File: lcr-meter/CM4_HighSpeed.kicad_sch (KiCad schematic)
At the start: 10 parts, among them J15 Conn_01x22_Female, J16 Conn_01x22_Female, J22 690-019-298-412, J6 THD-02-R, U12 RT9742SNGV

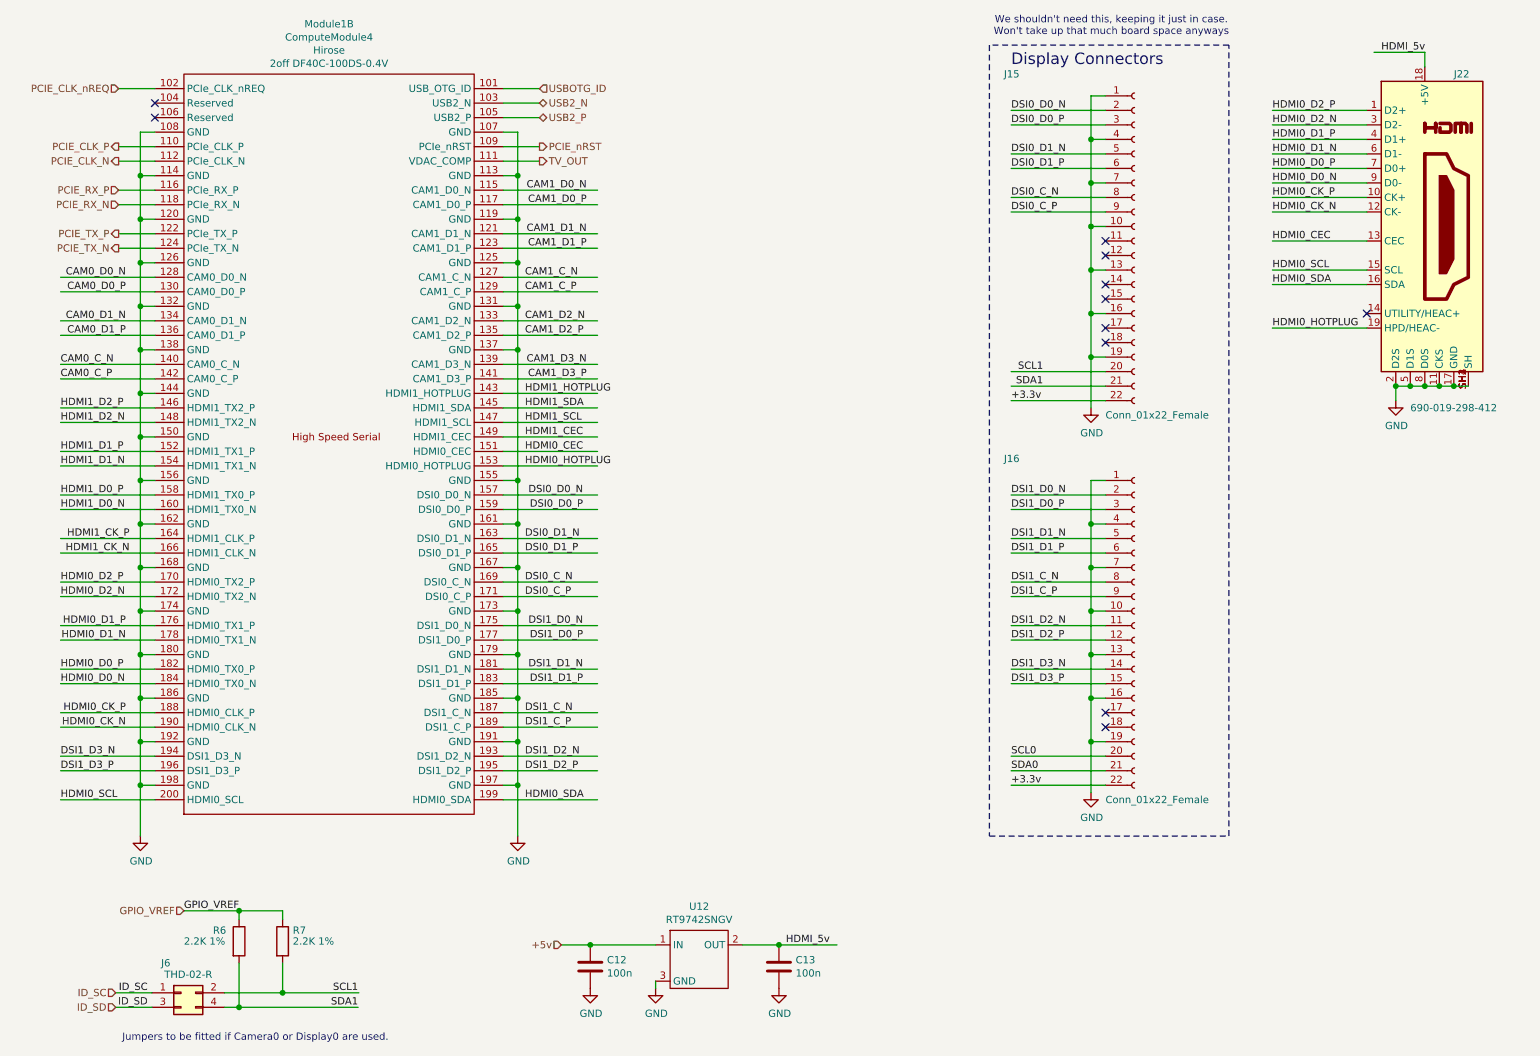
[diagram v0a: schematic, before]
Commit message: Progress, removal of unnecessary components
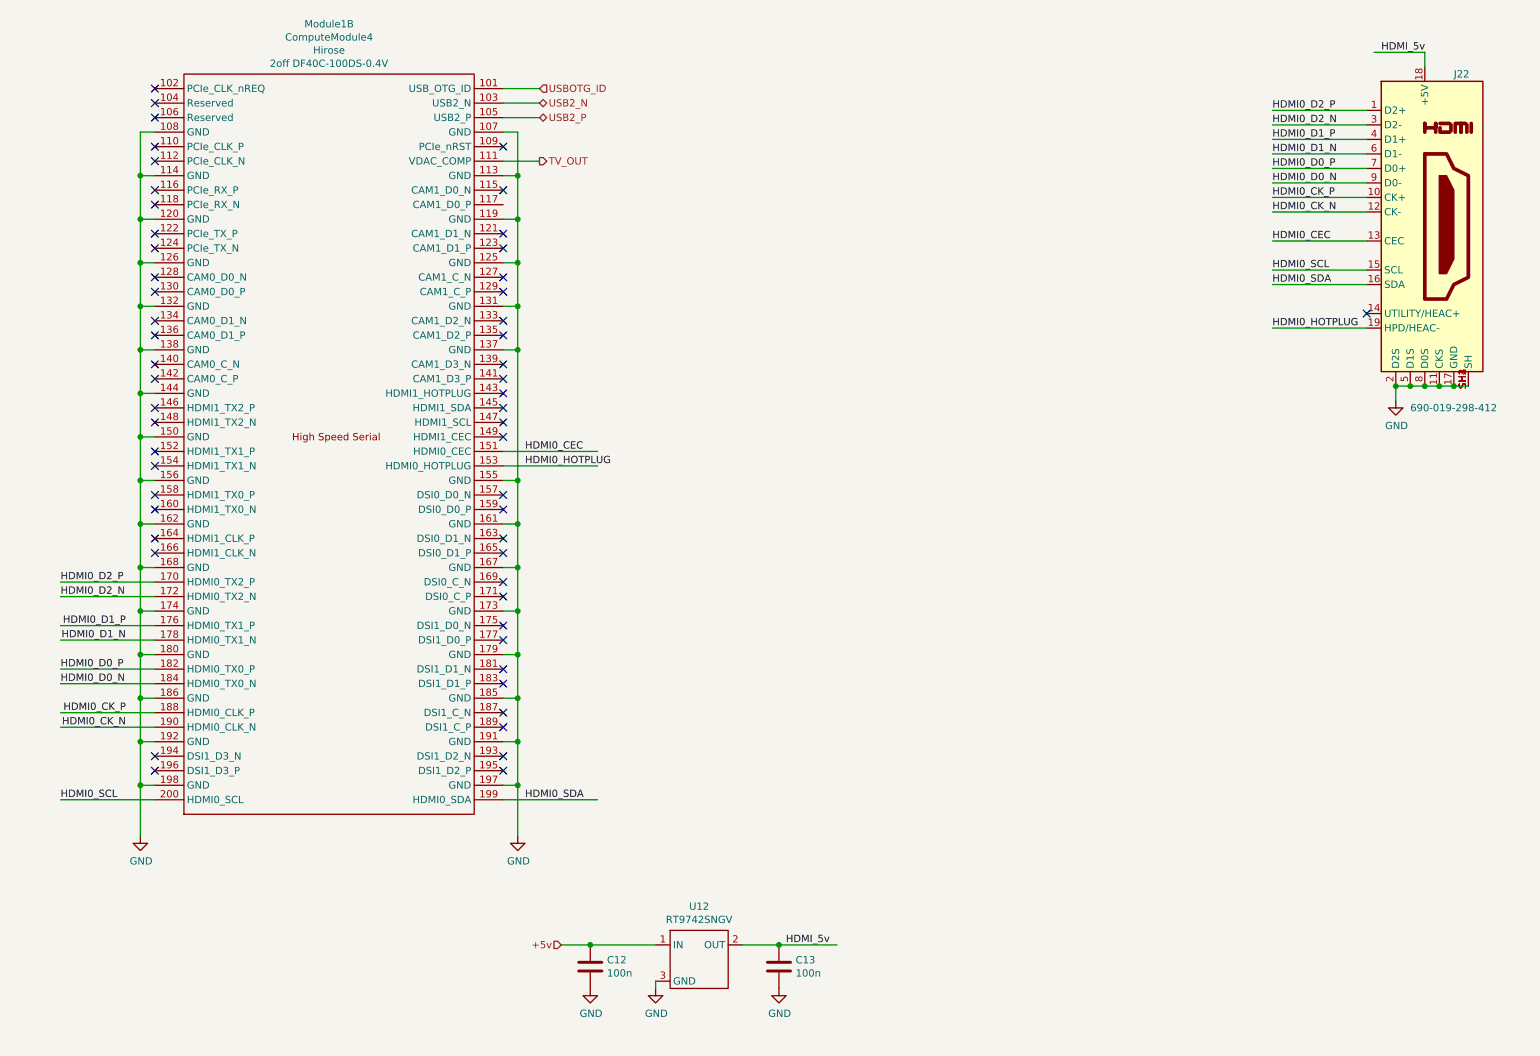
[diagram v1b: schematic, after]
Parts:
- removed J15, J16: Conn_01x22_Female, CM4IO:Hirose_FH12-22S-0.5SH_1x22-1MP_P0.50mm_Horizontal, symbol Connector:Conn_01x22_Female
- removed J6: THD-02-R, Connector_PinHeader_2.54mm:PinHeader_2x02_P2.54mm_Vertical, symbol Connector_Generic:Conn_02x02_Odd_Even
- removed R6, R7: 2.2K 1%, Resistor_SMD:R_0402_1005Metric, symbol Device:R
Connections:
- net CAM0_C_N: no longer names the net of Module1.140 (CAM0_C_N)
- net CAM0_C_P: no longer names the net of Module1.142 (CAM0_C_P)
- net CAM0_D0_N: no longer names the net of Module1.128 (CAM0_D0_N)
- net CAM0_D0_P: no longer names the net of Module1.130 (CAM0_D0_P)
- net CAM0_D1_N: no longer names the net of Module1.134 (CAM0_D1_N)
- net CAM0_D1_P: no longer names the net of Module1.136 (CAM0_D1_P)
- net CAM1_C_N: no longer names the net of Module1.127 (CAM1_C_N)
- net CAM1_C_P: no longer names the net of Module1.129 (CAM1_C_P)
- net CAM1_D0_N: no longer names the net of Module1.115 (CAM1_D0_N)
- net CAM1_D0_P: no longer names the net of Module1.117 (CAM1_D0_P)
- net CAM1_D1_N: no longer names the net of Module1.121 (CAM1_D1_N)
- net CAM1_D1_P: no longer names the net of Module1.123 (CAM1_D1_P)
- net CAM1_D2_N: no longer names the net of Module1.133 (CAM1_D2_N)
- net CAM1_D2_P: no longer names the net of Module1.135 (CAM1_D2_P)
- net CAM1_D3_N: no longer names the net of Module1.139 (CAM1_D3_N)
- net CAM1_D3_P: no longer names the net of Module1.141 (CAM1_D3_P)
- net DSI0_C_N: no longer names the net of Module1.169 (DSI0_C_N)
- net DSI0_C_P: no longer names the net of Module1.171 (DSI0_C_P)
- net DSI0_D0_N: no longer names the net of Module1.157 (DSI0_D0_N)
- net DSI0_D0_P: no longer names the net of Module1.159 (DSI0_D0_P)
- net DSI0_D1_N: no longer names the net of Module1.163 (DSI0_D1_N)
- net DSI0_D1_P: no longer names the net of Module1.165 (DSI0_D1_P)
- net DSI1_C_N: no longer names the net of Module1.187 (DSI1_C_N)
- net DSI1_C_P: no longer names the net of Module1.189 (DSI1_C_P)
- net DSI1_D0_N: no longer names the net of Module1.175 (DSI1_D0_N)
- net DSI1_D0_P: no longer names the net of Module1.177 (DSI1_D0_P)
- net DSI1_D1_N: no longer names the net of Module1.181 (DSI1_D1_N)
- net DSI1_D1_P: no longer names the net of Module1.183 (DSI1_D1_P)
- net DSI1_D2_N: no longer names the net of Module1.193 (DSI1_D2_N)
- net DSI1_D2_P: no longer names the net of Module1.195 (DSI1_D2_P)
- net DSI1_D3_N: no longer names the net of Module1.194 (DSI1_D3_N)
- net DSI1_D3_P: no longer names the net of Module1.196 (DSI1_D3_P)
- net HDMI1_CEC: no longer names the net of Module1.149 (HDMI1_CEC)
- net HDMI1_CK_N: no longer names the net of Module1.166 (HDMI1_CLK_N)
- net HDMI1_CK_P: no longer names the net of Module1.164 (HDMI1_CLK_P)
- net HDMI1_D0_N: no longer names the net of Module1.160 (HDMI1_TX0_N)
- net HDMI1_D0_P: no longer names the net of Module1.158 (HDMI1_TX0_P)
- net HDMI1_D1_N: no longer names the net of Module1.154 (HDMI1_TX1_N)
- net HDMI1_D1_P: no longer names the net of Module1.152 (HDMI1_TX1_P)
- net HDMI1_D2_N: no longer names the net of Module1.148 (HDMI1_TX2_N)
- net HDMI1_D2_P: no longer names the net of Module1.146 (HDMI1_TX2_P)
- net HDMI1_HOTPLUG: no longer names the net of Module1.143 (HDMI1_HOTPLUG)
- net HDMI1_SCL: no longer names the net of Module1.147 (HDMI1_SCL)
- net HDMI1_SDA: no longer names the net of Module1.145 (HDMI1_SDA)
- net PCIE_CLK_N: no longer names the net of Module1.112 (PCIe_CLK_N)
- net PCIE_CLK_P: no longer names the net of Module1.110 (PCIe_CLK_P)
- net PCIE_CLK_nREQ: no longer names the net of Module1.102 (PCIe_CLK_nREQ)
- net PCIE_RX_N: no longer names the net of Module1.118 (PCIe_RX_N)
- net PCIE_RX_P: no longer names the net of Module1.116 (PCIe_RX_P)
- net PCIE_TX_N: no longer names the net of Module1.124 (PCIe_TX_N)
- net PCIE_TX_P: no longer names the net of Module1.122 (PCIe_TX_P)
- net PCIE_nRST: no longer names the net of Module1.109 (PCIe_nRST)
- no-connect marks 11 -> 54
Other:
- note removed: "Display Connectors"
- note removed: "Jumpers to be fitted if Camera0 or Display0 are used."
- note removed: "We shouldn't need this, keeping it just in case. Won't take up that much board space anyways"

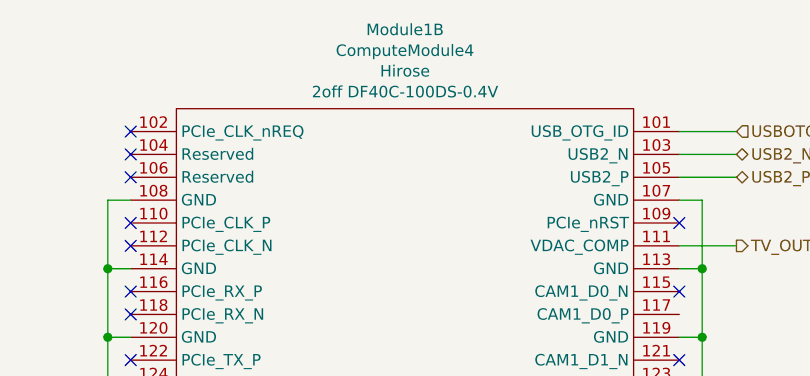
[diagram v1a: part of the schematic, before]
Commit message: Addressable LED test board
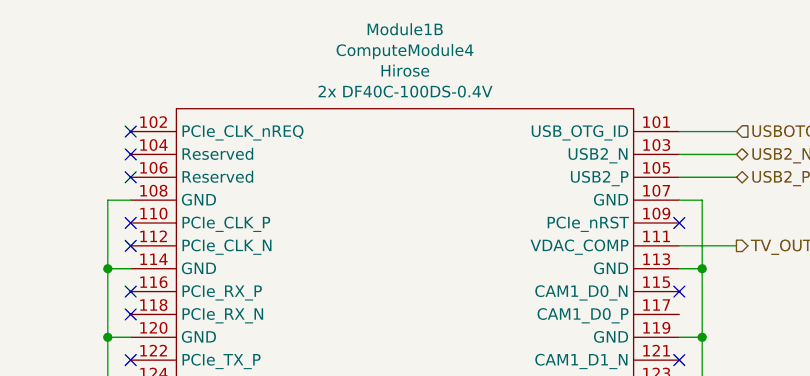
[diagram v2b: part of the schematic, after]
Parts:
- Module1: Field5 2off DF40C-100DS-0.4V -> 2x DF40C-100DS-0.4V
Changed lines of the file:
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@@
 			)
 		)
-		(property "Description" ""
+		(property "Description" "Power symbol creates a global label with name \"GND\" , ground"
 			(at 259.08 81.28 0)
 			(effects
@@
 			)
 		)
-		(property "Description" ""
+		(property "Description" "Power symbol creates a global label with name \"GND\" , ground"
 			(at 105.41 157.48 0)
 			(effects
@@
 			)
 		)
-		(property "Description" ""
+		(property "Description" "Power symbol creates a global label with name \"GND\" , ground"
 			(at 39.37 157.48 0)
 			(effects
@@
 			)
 		)
-		(property "Datasheet" "https://www.tme.eu/Document/f15dffbcfad8545e17826f72d36911c8/206A-SEAN-R03.pdf"
+		(property "Datasheet" "https://en.wikipedia.org/wiki/HDMI"
 			(at 264.795 50.8 0)
 			(effects
@@
 			)
 		)
-		(property "Description" ""
+		(property "Description" "HDMI 1.4+ type A connector"
 			(at 264.16 50.8 0)
 			(effects
@@
 			)
 		)
-		(property "Datasheet" "https://search.murata.co.jp/Ceramy/image/img/A01X/G101/ENG/GRM155R71C104KA88-01.pdf"
+		(property "Datasheet" "~"
 			(at 151.13 180.34 0)
 			(effects
@@
 			)
 		)
-		(property "Description" ""
+		(property "Description" "Unpolarized capacitor"
 			(at 151.13 180.34 0)
 			(effects
@@
 			)
 		)
-		(property "Datasheet" "https://search.murata.co.jp/Ceramy/image/img/A01X/G101/ENG/GRM155R71C104KA88-01.pdf"
+		(property "Datasheet" "~"
 			(at 118.11 180.34 0)
 			(effects
@@
 			)
 		)
-		(property "Description" ""
+		(property "Description" "Unpolarized capacitor"
 			(at 118.11 180.34 0)
 			(effects
@@
 			)
 		)
-		(property "Description" ""
+		(property "Description" "Power symbol creates a global label with name \"GND\" , ground"
 			(at 151.13 184.15 0)
 			(effects
@@
 			)
 		)
-		(property "Description" ""
+		(property "Description" "Power symbol creates a global label with name \"GND\" , ground"
 			(at 118.11 184.15 0)
 			(effects
@@
 			)
 		)
-		(property "Description" ""
+		(property "Description" "Power symbol creates a global label with name \"GND\" , ground"
 			(at 129.54 184.15 0)
 			(effects
@@
 			)
 		)
-		(property "Field5" "2off DF40C-100DS-0.4V"
+		(property "Field5" "2x DF40C-100DS-0.4V"
 			(at 72.39 22.2758 0)
 			(effects
